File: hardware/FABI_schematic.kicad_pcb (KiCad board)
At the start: 2 copper layers, 81 x 55 mm, 62 parts, among them J1 Conn_01x02_Pin, J11 009159005551906, J11_GND1 Conn_01x01_Male, J11_VDD1 Conn_01x01_Male, J11_data1 Conn_01x01_Male, J12 Conn_01x04_Socket, J2 display_connector_91601-304LF, J3 54601-906WPLF, J4 54-00174 / FC68125, J5 54-00174 / FC68125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

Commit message: Moved U4 Component needed for External Sensor in order to gain more space
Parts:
- added C13: 4.7uF, Capacitor_SMD:C_0603_1608Metric_Pad1.08x0.95mm_HandSolder, F.Cu at (82.1, 57.1)
- added C14: 4.7uF, Capacitor_SMD:C_0603_1608Metric_Pad1.08x0.95mm_HandSolder, F.Cu at (82.1, 59.6)
- added D5: 10BQ015, Diode_SMD:D_SMB_Handsoldering, F.Cu at (93.6, 66.3)
- added J7: JST PH2P ST, Connector_JST:JST_PH_B2B-PH-K_1x02_P2.00mm_Vertical, F.Cu at (91.3, 71.8)
- added Q2: PMOS AS3401, Package_TO_SOT_SMD:TSOT-23_HandSoldering, F.Cu at (99.3, 58.2)
- added R11: 10k, Resistor_SMD:R_0603_1608Metric_Pad0.98x0.95mm_HandSolder, F.Cu at (82.1, 62.1)
- added R12: 2k, Resistor_SMD:R_0603_1608Metric_Pad0.98x0.95mm_HandSolder, F.Cu at (82.1, 64.6)
- added R13: 100k, Resistor_SMD:R_0603_1608Metric_Pad0.98x0.95mm_HandSolder, F.Cu at (82.1, 67.1)
- added R14: 100k, Resistor_SMD:R_0603_1608Metric_Pad0.98x0.95mm_HandSolder, F.Cu at (82.1, 69.6)
- added S1: 450404015514, BMS:450404015514, F.Cu at (90.0, 58.9)
- added TP2: TestPoint_Probe, TestPoint:TestPoint_THTPad_D2.0mm_Drill1.0mm, F.Cu at (86.3, 65.6)
- added TP3: TestPoint_Probe, TestPoint:TestPoint_THTPad_D2.0mm_Drill1.0mm, F.Cu at (86.3, 69.6)
- added TP4: TestPoint_Probe, TestPoint:TestPoint_THTPad_D2.0mm_Drill1.0mm, F.Cu at (86.3, 73.7)
- added U9: MCP73831-2, Package_TO_SOT_SMD:SOT-23-5_HandSoldering, F.Cu at (99.2, 71.5)
- moved U4 4.42 mm to (107.0, 101.5)
- moved C3 4.42 mm to (110.0, 101.5)
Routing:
- net GNDA: track 66.1 -> 59.6 mm
- net +3.3VADC: track 161.8 -> 158.4 mm
- net /SCL: track 92.5 -> 95.3 mm
- net /SDA: track 104.2 -> 106.9 mm
- net VCC: track 157.5 -> 160.1 mm
- net /EXT1: track 101.7 -> 103.4 mm
- net GND: track 108.3 -> 108.6 mm, vias 166 -> 162
- removed copper zone on B.Cu, net GND
- removed copper zone on F.Cu, net GND

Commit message: Added all prev. modifications to SRC_v3.0 update by ChrisVeigl; Removed redundant LDO; Most components of the BMS is on the board except for testpoints and battery measurement resistors; Wired most components;
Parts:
- moved S1 90.6 mm to (169.2, 102.8)
- moved R11 39.3 mm to (112.5, 87.0), turned to -90 degrees
- moved C14 39.0 mm to (106.5, 90.0), turned to -90 degrees
- moved Q2 37.6 mm to (107.0, 95.0), turned to -90 degrees
- moved C13 37.3 mm to (98.5, 90.5)
- moved R12 36.3 mm to (108.0, 90.0), turned to 90 degrees
- moved D5 32.5 mm to (111.0, 93.8), turned to 90 degrees
- moved J7 17.6 mm to (101.0, 86.5)
- moved U9 17.5 mm to (109.0, 86.0)
- moved TP4 0.33 mm to (86.3, 74.0)
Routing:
- net V_PWR_SWITCH: track 0.00 -> 65.5 mm, vias 0 -> 1
- net V_BATT: track 0.00 -> 32.7 mm, vias 0 -> 2
- net VBUS: track 60.8 -> 82.7 mm, vias 1 -> 3
- net Net-(U9-PROG): track 0.00 -> 5.01 mm
- net VCC: track 160.1 -> 159.3 mm
- net GND: vias 162 -> 145
- added copper zone on B.Cu, net GND
- added copper zone on F.Cu, net GND

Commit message: Ran DRC and fixued some warnings
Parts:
- moved R13 18.8 mm to (99.8, 73.5)
- moved R14 18.8 mm to (99.8, 76.0)
- moved TP2 18.8 mm to (104.0, 72.0)
- moved TP3 18.8 mm to (104.0, 76.0)
- moved TP4 18.8 mm to (104.0, 80.4)
- moved S1 3.99 mm to (165.5, 101.5), turned to -90 degrees
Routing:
- net GND: track 108.6 -> 113.4 mm, vias 145 -> 149
- net VSYS: track 107.3 -> 105.2 mm

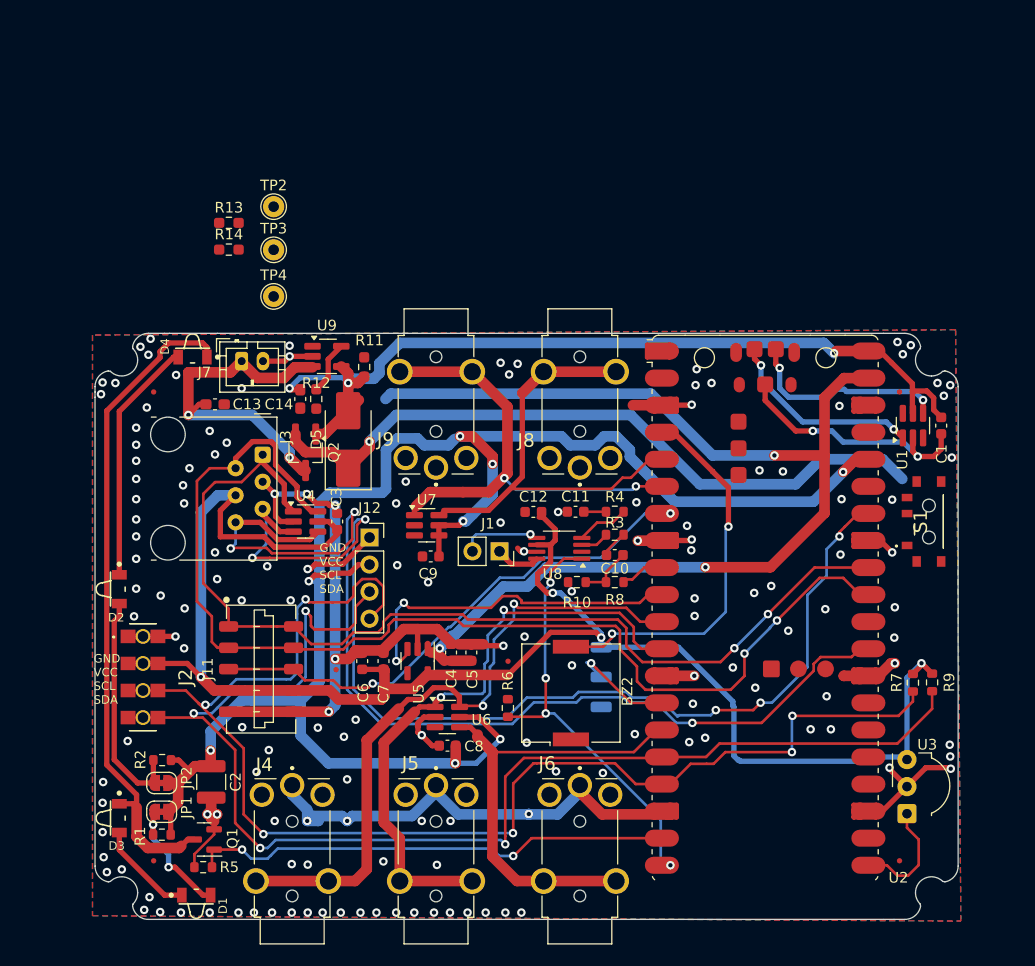
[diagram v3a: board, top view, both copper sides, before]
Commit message: Moved S-Diode over to PWR_Switch (far right); Rewired all the added components; Moved R7 & R9 so TP3 + PWR_Switch + S-Diode would have space; Made space for TP2 & TP4 and wired them accordingly; Ran DRC with the only error -Missing connection between Zone GND on F.Cu and B.Cu-;
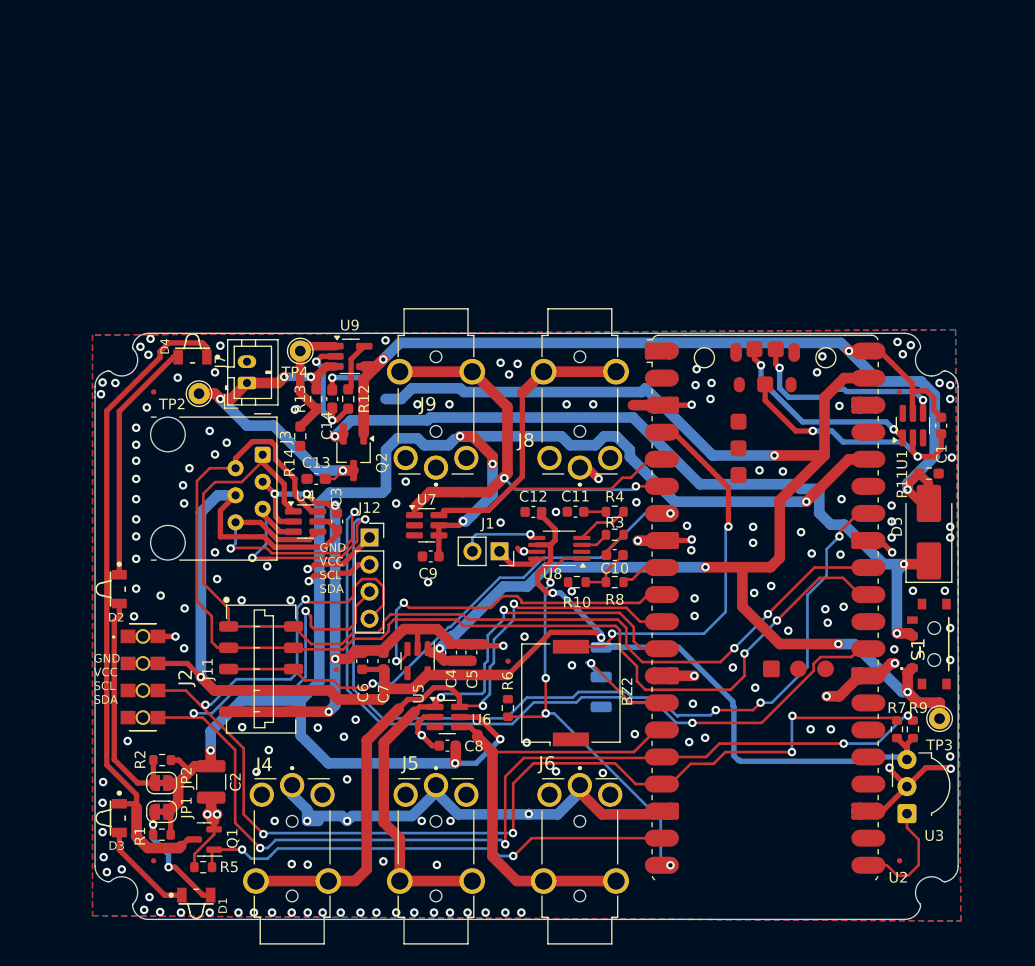
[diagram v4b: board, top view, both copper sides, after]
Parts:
- moved TP3 76.4 mm to (166.5, 120.0)
- moved D5 55.2 mm to (165.5, 102.5)
- moved R11 53.9 mm to (165.5, 97.0), turned to 180 degrees
- moved TP2 18.9 mm to (97.0, 89.5)
- moved R14 18.8 mm to (106.5, 93.5), turned to 90 degrees
- moved R13 18.5 mm to (108.0, 90.0), turned to 90 degrees
- moved C13 11.8 mm to (108.0, 97.5), turned to 180 degrees
- moved S1 11.5 mm to (166.0, 113.0)
- moved TP4 5.70 mm to (106.5, 85.5)
- moved R9 4.75 mm to (164.0, 121.0), turned to -90 degrees
- moved R7 4.62 mm to (162.5, 121.0), turned to -90 degrees
- moved Q2 4.50 mm to (111.5, 95.0)
- moved C14 3.00 mm to (109.5, 90.0)
- moved R12 3.00 mm to (111.0, 90.0)
- moved U9 2.15 mm to (111.2, 86.0)
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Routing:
- net VSYS: track 105.2 -> 135.7 mm, vias 3 -> 5
- net VBUS: track 82.7 -> 102.9 mm, vias 3 -> 4
- net V_BATT_MEASURE: track 0.00 -> 11.8 mm
- net GND: track 113.4 -> 124.5 mm, vias 149 -> 172
- net +3.3VADC: track 158.4 -> 149.7 mm, vias 4 -> 3
- net V_PWR_SWITCH: track 65.5 -> 72.8 mm, vias 1 -> 3
- net /SDA_INT: track 125.2 -> 121.7 mm, vias 4 -> 6
- net /SCL_INT: track 127.3 -> 124.5 mm
- net V_BATT: track 32.7 -> 32.9 mm, vias 2 -> 4

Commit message: Ran DRC again and fixed the issues of yesterday's (19.11.24) commit, the issues lied in two ground islands on the B.Cu that were not connected; Rereouted BUTTON4 route in the area of J8 and the NET-(U1-I/03) route in the area of TP2, the USB_DM;
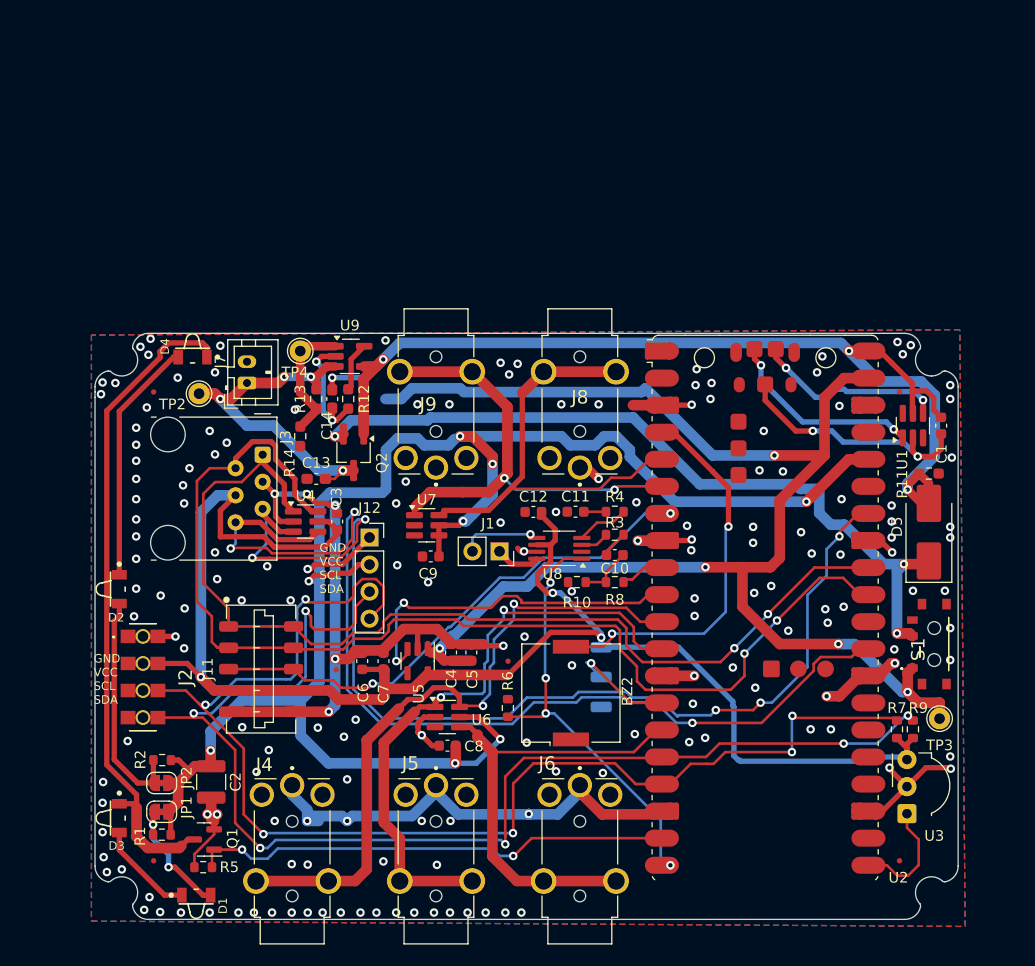
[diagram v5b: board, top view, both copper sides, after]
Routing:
- net Net-(U1-I/O3): track 19.6 -> 18.1 mm
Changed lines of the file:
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@@
 		(tags "resistor")
 		(property "Reference" "R7"
-			(at -2 0 360)
+			(at -2 0 0)
 			(layer "F.SilkS")
 			(effects
@@
 		)
 		(property "Digikey" "1292-WR06X472JTLCT-ND"
-			(at 0 0 360)
+			(at 0 0 0)
 			(layer "F.Fab")
 			(hide yes)
@@
 		)
 		(property "Farnell" "3994558"
-			(at 0 0 360)
+			(at 0 0 0)
 			(layer "F.Fab")
 			(hide yes)
@@
 		)
 		(property "Mouser" "756-WCR0603-4K7FI"
-			(at 0 0 360)
+			(at 0 0 0)
 			(layer "F.Fab")
 			(hide yes)
@@
 		)
 		(property "RS Components" "199-5594"
-			(at 0 0 360)
+			(at 0 0 0)
 			(layer "F.Fab")
 			(hide yes)
@@
 		(tags "resistor")
 		(property "Reference" "R9"
-			(at -2 -0.5 360)
+			(at -2 -0.5 0)
 			(layer "F.SilkS")
 			(effects
@@
 		)
 		(property "Digikey" "1292-WR06X472JTLCT-ND"
-			(at 0 0 360)
+			(at 0 0 0)
 			(layer "F.Fab")
 			(hide yes)
@@
 		)
 		(property "Farnell" "3994558"
-			(at 0 0 360)
+			(at 0 0 0)
 			(layer "F.Fab")
 			(hide yes)
@@
 		)
 		(property "Mouser" "756-WCR0603-4K7FI"
-			(at 0 0 360)
+			(at 0 0 0)
 			(layer "F.Fab")
 			(hide yes)
@@
 		)
 		(property "RS Components" "199-5594"
-			(at 0 0 360)
+			(at 0 0 0)
 			(layer "F.Fab")
 			(hide yes)
@@
 		(fp_arc
 			(start 10.579676 25.189937)
-			(mid 10.494803 25.356771)
+			(mid 10.494812 25.356783)
 			(end 10.363318 25.49)
 			(stroke
@@
 		(tags "Connector")
 		(property "Reference" "J8"
-			(at -5.04 4.06 0)
+			(at 0 0 0)
 			(layer "F.SilkS")
 			(effects
@@
 		(tags "capacitor handsolder")
 		(property "Reference" "C13"
-			(at 0 1.5 360)
+			(at 0 1.5 0)
 			(layer "F.SilkS")
 			(effects
@@
 		)
 		(property "Value" "4.7uF"
-			(at 0 1.43 360)
+			(at 0 1.43 0)
 			(layer "F.Fab")
 			(effects
@@
 		)
 		(fp_text user "${REFERENCE}"
-			(at 0 0 360)
+			(at 0 0 0)
 			(layer "F.Fab")
 			(effects
@@
 		)
 		(property "Value" "10k"
-			(at 0 1.43 360)
+			(at 0 1.43 0)
 			(layer "F.Fab")
 			(effects
@@
 		)
 		(fp_text user "${REFERENCE}"
-			(at 0 0 360)
+			(at 0 0 0)
 			(layer "F.Fab")
 			(effects
@@
 	)
 	(via
-		(at 166.5 88.5)
-		(size 0.8)
-		(drill 0.4)
-		(layers "F.Cu" "B.Cu")
-		(free yes)
-		(net 1)
-	)
-	(via
 		(at 93.4 108.45)
 		(size 0.8)
@@
 	)
 	(via
+		(at 150 93)
+		(size 0.8)
+		(drill 0.4)
+		(layers "F.Cu" "B.Cu")
+		(free yes)
+		(net 1)
+	)
+	(via
 		(at 99.6 94.1)
 		(size 0.8)
@@
 	)
 	(via
-		(at 134 90.5)
+		(at 134.5 90.5)
 		(size 0.8)
 		(drill 0.4)
@@
 	)
 	(via
-		(at 131.5 90.5)
+		(at 131 90.5)
 		(size 0.8)
 		(drill 0.4)
@@
 	)
 	(segment
-		(start 135.69 98.44)
-		(end 136.74 97.39)
+		(start 124.079 100.457)
+		(end 126.096 98.44)
+		(width 0.25)
+		(layer "F.Cu")
+		(net 11)
+	)
+	(segment
+		(start 135.675 97.39)
+		(end 137.54 97.39)
 		(width 0.25)
 		(layer "F.Cu")
@@
 	)
 	(segment
-		(start 137.54 97.39)
-		(end 139.27 95.66)
+		(start 139.27 95.66)
+		(end 141.24 95.66)
 		(width 0.25)
 		(layer "F.Cu")
@@
 	)
 	(segment
-		(start 124.079 100.457)
-		(end 126.096 98.44)
-		(width 0.25)
-		(layer "F.Cu")
-		(net 11)
-	)
-	(segment
 		(start 124.180056 100.457)
 		(end 127.34 97.297056)
@@
 	)
 	(segment
-		(start 126.096 98.44)
-		(end 135.69 98.44)
-		(width 0.25)
+		(start 127.34 97.297056)
+		(end 127.34 89.44)
+		(width 0.5)
 		(layer "F.Cu")
 		(net 11)
 	)
 	(segment
-		(start 127.34 97.297056)
-		(end 127.34 89.44)
-		(width 0.5)
+		(start 134.625 98.44)
+		(end 135.675 97.39)
+		(width 0.25)
 		(layer "F.Cu")
 		(net 11)
 	)
 	(segment
-		(start 136.74 97.39)
-		(end 137.54 97.39)
+		(start 126.096 98.44)
+		(end 134.625 98.44)
 		(width 0.25)
 		(layer "F.Cu")
@@
 	)
 	(segment
-		(start 139.27 95.66)
-		(end 141.24 95.66)
+		(start 137.54 97.39)
+		(end 139.27 95.66)
 		(width 0.25)
 		(layer "F.Cu")
@@
 	)
 	(segment
+		(start 141.24 98.2)
+		(end 136.31825 98.2)
+		(width 0.25)
+		(layer "F.Cu")
+		(net 14)
+	)
+	(segment
 		(start 115.84 87.44)
 		(end 122.64 87.44)
@@
 	)
 	(segment
-		(start 141.24 98.2)
-		(end 138 98.2)
+		(start 136.31825 98.2)
+		(end 136 98.51825)
 		(width 0.25)
 		(layer "F.Cu")
@@
 	)
 	(via
-		(at 138 98.2)
+		(at 136 98.51825)
 		(size 0.8)
 		(drill 0.4)
@@
 	)
 	(segment
-		(start 138 98.2)
-		(end 137.68175 98.51825)
+		(start 136 98.51825)
+		(end 126.736827 98.51825)
 		(width 0.25)
 		(layer "B.Cu")
@@
 	)
 	(segment
-		(start 137.68175 98.51825)
-		(end 126.736827 98.51825)
-		(width 0.25)
-		(layer "B.Cu")
-		(net 14)
-	)
-	(segment
 		(start 102.97 95.83)
 		(end 101 97.8)
@@
 	)
 	(segment
-		(start 151.49 87.09)
-		(end 151.13 86.73)
+		(start 152.09 87.09)
+		(end 151.13 86.13)
 		(width 0.5)
 		(layer "F.Cu")
@@
 	)
 	(segment
-		(start 164.95 90.1)
-		(end 164.95 91.3625)
+		(start 151.13 86.13)
+		(end 151.13 85.33)
 		(width 0.5)
 		(layer "F.Cu")
@@
 	)
 	(segment
-		(start 151.13 86.73)
-		(end 151.13 85.33)
+		(start 164.95 90.1)
+		(end 164.95 91.3625)
 		(width 0.5)
 		(layer "F.Cu")
@@
 	)
 	(via
-		(at 151.49 87.09)
+		(at 152.09 87.09)
 		(size 0.8)
 		(drill 0.4)
@@
 	)
 	(segment
-		(start 157.542082 89.09)
-		(end 157.752082 89.3)
+		(start 152.09 87.09)
+		(end 154.84 89.84)
 		(width 0.5)
 		(layer "B.Cu")
@@
 	)
 	(segment
-		(start 156.837918 89.09)
-		(end 157.542082 89.09)
+		(start 164.15 89.3)
+		(end 164.95 90.1)
 		(width 0.5)
 		(layer "B.Cu")
@@
 	)
 	(segment
-		(start 151.49 89.00005)
-		(end 152.32995 89.84)
-		(width 0.5)
-		(layer "B.Cu")
-		(net 43)
-	)
-	(segment
-		(start 152.32995 89.84)
+		(start 154.84 89.84)
 		(end 156.087918 89.84)
 		(width 0.5)
@@
 	)
 	(segment
-		(start 151.49 87.09)
-		(end 151.49 89.00005)
+		(start 156.837918 89.09)
+		(end 157.542082 89.09)
 		(width 0.5)
 		(layer "B.Cu")
@@
 	)
 	(segment
-		(start 164.15 89.3)
-		(end 164.95 90.1)
+		(start 157.542082 89.09)
+		(end 157.752082 89.3)
 		(width 0.5)
 		(layer "B.Cu")
@@
 		(polygon
 			(pts
-				(xy 168 83.5) (xy 87 84) (xy 87 138.5) (xy 168.5 139)
+				(xy 168.400909 83.500893) (xy 86.900909 84.000893) (xy 86.900909 139.000893) (xy 168.900909 139.500893)
 			)
 		)

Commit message: Added solder jumper between BAT and p-MOS; Rewired battery level measurem. to GPIO pin in order to have it off when not needed; Changed all Rs into EU Rs; Renamed all components for them to be uniform; Removed Schottky since Pico W has its own built in as well as pulldown R; Changed p-MOSFET to recommended p-MOS in 28 page datasheet (Pico W); Changed Footprint of Audio AMP, rewired too;
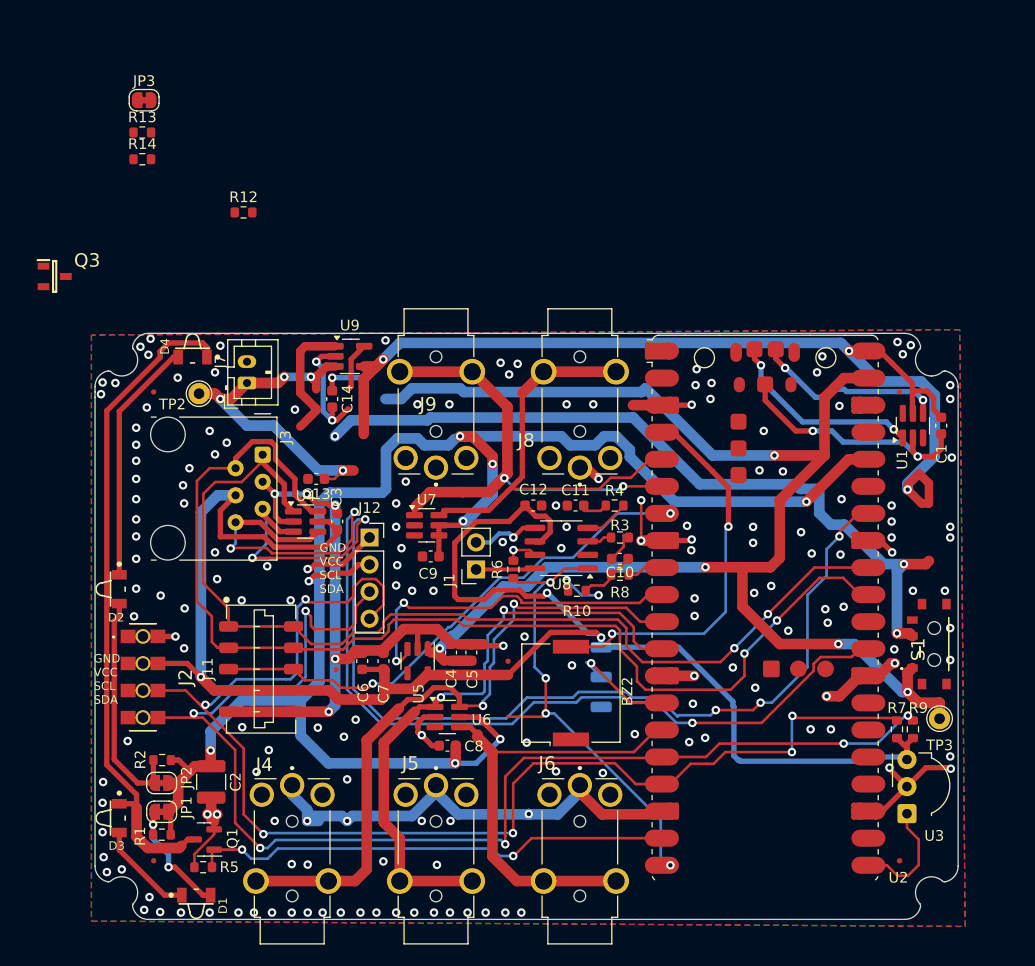
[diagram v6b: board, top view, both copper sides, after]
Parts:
- removed D5: 10BQ015, Diode_SMD:D_SMB_Handsoldering
- removed Q2: PMOS AS3401, Package_TO_SOT_SMD:TSOT-23_HandSoldering
- removed R11: 10k, Resistor_SMD:R_0603_1608Metric_Pad0.98x0.95mm_HandSolder
- removed TP4: TestPoint_Probe, TestPoint:TestPoint_THTPad_D2.0mm_Drill1.0mm
- added JP3: SolderJumper_2_Bridged, Jumper:SolderJumper-2_P1.3mm_Bridged_RoundedPad1.0x1.5mm, F.Cu at (91.8, 62.0)
- added Q3: DMG2305UXQ-7, p-MOS:SOT96P240X110-3N, F.Cu at (83.5, 78.5)
- C13, C14: value 4.7uF -> 4.7u; footprint Capacitor_SMD:C_0603_1608Metric_Pad1.08x0.95mm_HandSolder -> Capacitor_SMD:C_0603_1608Metric
- R12: value 2k -> 3k3; footprint Resistor_SMD:R_0603_1608Metric_Pad0.98x0.95mm_HandSolder -> Resistor_SMD:R_0603_1608Metric
- R13, R14: footprint Resistor_SMD:R_0603_1608Metric_Pad0.98x0.95mm_HandSolder -> Resistor_SMD:R_0603_1608Metric
- R6: value 10k -> 4k7
- U8: footprint Package_SO:MSOP-8_3x3mm_P0.65mm -> Package_SO:SOIC-8_3.9x4.9mm_P1.27mm
- moved R14 29.9 mm to (91.7, 67.5), turned to 0 degrees
- moved R13 29.9 mm to (91.7, 65.0), turned to 0 degrees
- moved R12 20.1 mm to (101.2, 72.5), turned to 0 degrees
- moved R6 13.0 mm to (126.5, 106.0), turned to -90 degrees
- moved J1 2.78 mm to (123.0, 106.0), turned to 180 degrees
- moved R8 0.84 mm to (136.5, 106.5)
- moved R10 0.81 mm to (132.5, 108.0)
- moved C12 0.60 mm to (128.4, 100.0), turned to 180 degrees
- moved C10 0.60 mm to (136.5, 105.0)
- moved R4 0.58 mm to (136.0, 100.0)
- moved C11 0.58 mm to (132.3, 100.0)
- moved R3 0.55 mm to (136.5, 103.0)
- moved U8 0.19 mm to (131.0, 104.0)
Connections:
- C1 pad 1: VBUS -> V_PWR_SWITCH
- C14 pad 1: VBUS -> V_PWR_SWITCH
- C3 pad 2: GNDA -> GND
- C4 pad 2: GNDA -> GND
- C5 pad 2: GNDA -> GND
- C6 pad 2: GNDA -> GND
- C7 pad 2: GNDA -> GND
- J11 pad 5: GNDA -> GND
- J3 pad 3: GNDA -> GND
- NT2 pad 2: GNDA -> GND
- R12 pad 1: GND -> Net-(U9-PROG)
- R12 pad 2: Net-(U9-PROG) -> GND
- R13 pad 1: V_BATT_MEASURE -> V_BATT
- R13 pad 2: V_BATT -> V_BATT_MEASURE
- R14 pad 1: GND -> V_BATT_MEASURE
- R14 pad 2: V_BATT_MEASURE -> /LPW1/V_BATT_PIN
- R6 pad 1: /Audio_SD -> GND
- R6 pad 2: GND -> /Audio_SD
- TP2 pad 1: V_BATT -> Net-(JP3-A)
- U1 pad 5: VBUS -> V_PWR_SWITCH
- U2 pad 1: unconnected-(U2-GPIO0-Pad1) -> /V_BATT_PIN
- U2 pad 2: unconnected-(U2-GPIO1-Pad2) -> CHARGE_STAT
- U2 pad 40: VBUS -> V_PWR_SWITCH
- U4 pad 2: GNDA -> GND
- U5 pad 2: GNDA -> GND
- U9 pad 1: V_BATT_MEASURE -> CHARGE_STAT
- U9 pad 4: VBUS -> V_PWR_SWITCH
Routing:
- net VBUS: track 102.9 -> 0.00 mm, vias 4 -> 0
- net V_PWR_SWITCH: track 72.8 -> 174.8 mm, vias 3 -> 7
- net GND: track 124.5 -> 193.5 mm, vias 172 -> 184
- net GNDA: track 59.6 -> 0.00 mm, vias 5 -> 0
- net +3.3VADC: track 149.7 -> 167.4 mm
- net V_BATT_MEASURE: track 11.8 -> 0.00 mm
- net CHARGE_STAT: track 0.00 -> 11.8 mm
- net /Audio_SD: track 40.7 -> 45.1 mm
- net Net-(J1-Pin_1): track 4.31 -> 5.56 mm
- net Net-(U8-IN-): track 4.94 -> 4.26 mm
- net /Audio_Signal: track 5.26 -> 4.59 mm
- net Net-(C10-Pad1): track 4.85 -> 5.42 mm
